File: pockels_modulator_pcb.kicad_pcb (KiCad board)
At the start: 2 copper layers, 39.4 x 23.8 mm, 11 parts, among them J1 Conn_Coaxial

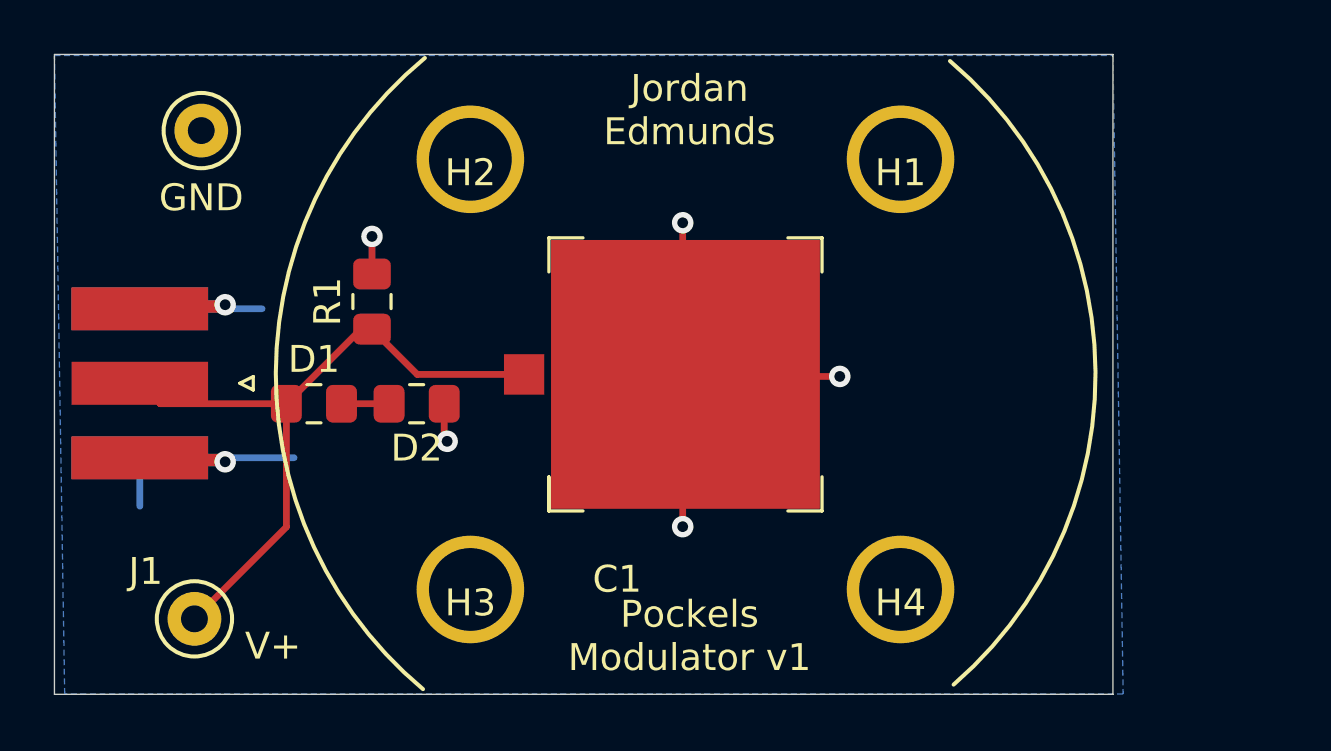
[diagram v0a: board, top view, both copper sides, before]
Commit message: revised pockels modulator PCB to include thermal vias, chip for thermal sensing, SMD connector
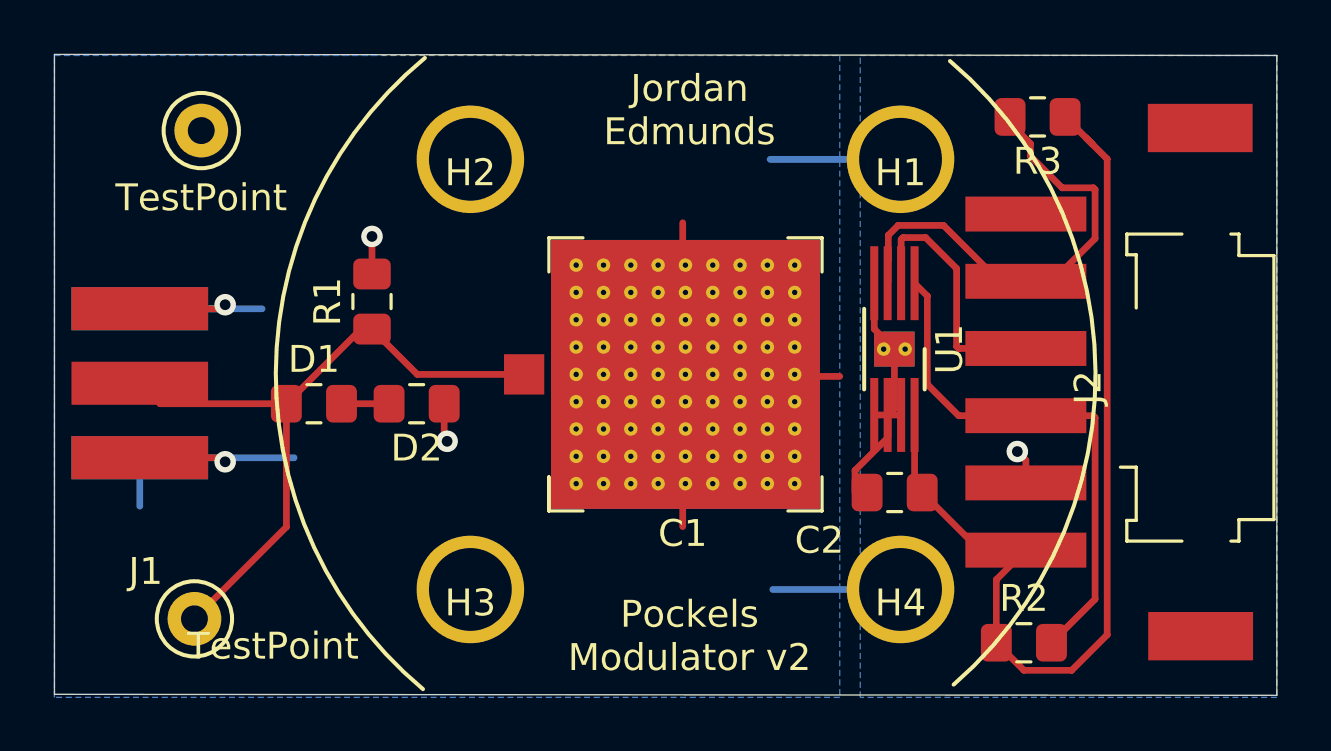
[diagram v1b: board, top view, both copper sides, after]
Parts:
- added C2: 100nF, Capacitor_SMD:C_0805_2012Metric_Pad1.15x1.40mm_HandSolder, F.Cu at (207.8, 104.4)
- added J2: Conn_01x06_Male, my_library_foot:S6B-XH-SM4-TB, F.Cu at (219.2, 109.7)
- added R2: 10k, Resistor_SMD:R_0805_2012Metric_Pad1.15x1.40mm_HandSolder, F.Cu at (212.6, 110.0)
- added R3: 10k, Resistor_SMD:R_0805_2012Metric_Pad1.15x1.40mm_HandSolder, F.Cu at (213.1, 90.4)
- added U1: MCP9804_DFN, Package_DFN_QFN:DFN-8-1EP_3x2mm_P0.5mm_EP1.3x1.5mm_HandSolder, F.Cu at (207.8, 99.1)
- C1: footprint my_library_foot:pockels_chip_10mm -> my_library_foot:pockels_chip_10mm_thermal
- TP1: value V+ -> TestPoint
- TP2: value GND -> TestPoint
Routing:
- net VDD: track 0.00 -> 37.5 mm
- net /SDA: track 0.00 -> 19.8 mm
- net /ALT: track 0.00 -> 17.7 mm
- net GNDD: track 0.00 -> 11.0 mm, vias 0 -> 1
- net /SCL: track 0.00 -> 9.70 mm
- net GND: track 41.4 -> 51.0 mm, vias 7 -> 4
- added copper zone on B.Cu, net GNDD
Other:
- board size 39.4 x 23.8 mm -> 45.5 x 23.8 mm
- board text added: "Pockels Modulator v2"
- board text removed: "Pockels Modulator v1"

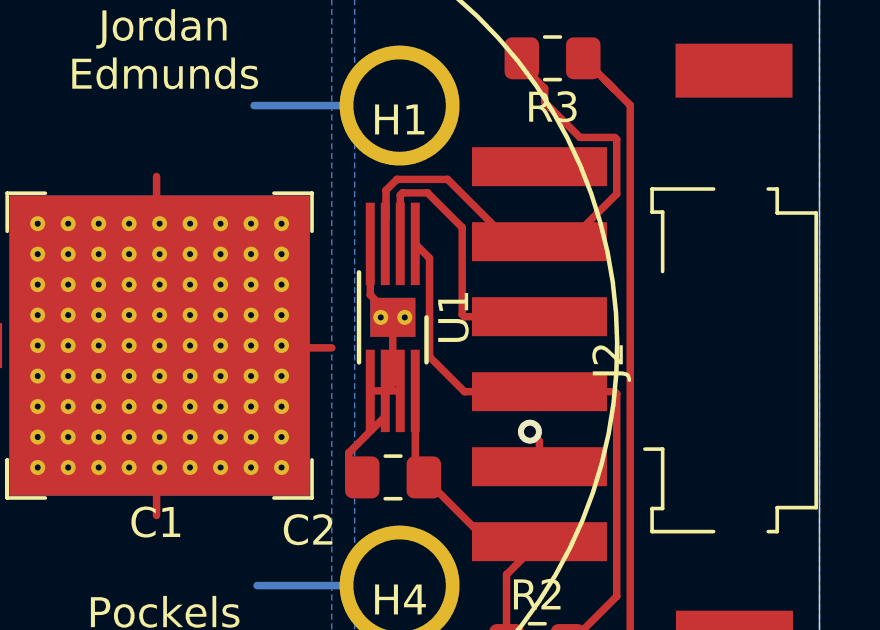
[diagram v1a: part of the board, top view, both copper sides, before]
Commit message: tweaked PCB in a manner I don't remember how. This is why you commit immediately after working.
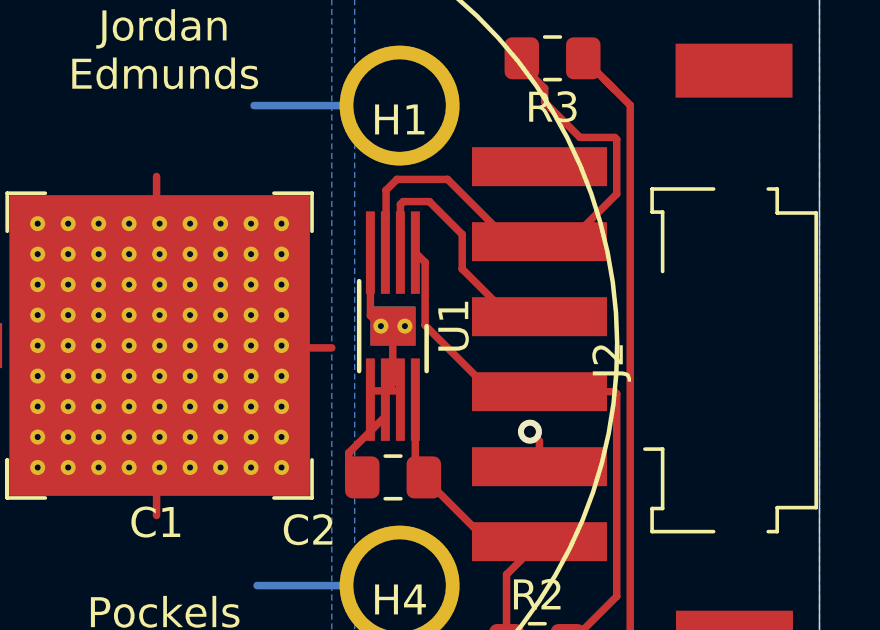
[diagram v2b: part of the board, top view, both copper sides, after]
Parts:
- moved U1 0.29 mm to (207.8, 99.4)
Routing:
- net /SCL: track 9.70 -> 8.55 mm
- net /SDA: track 19.8 -> 18.9 mm

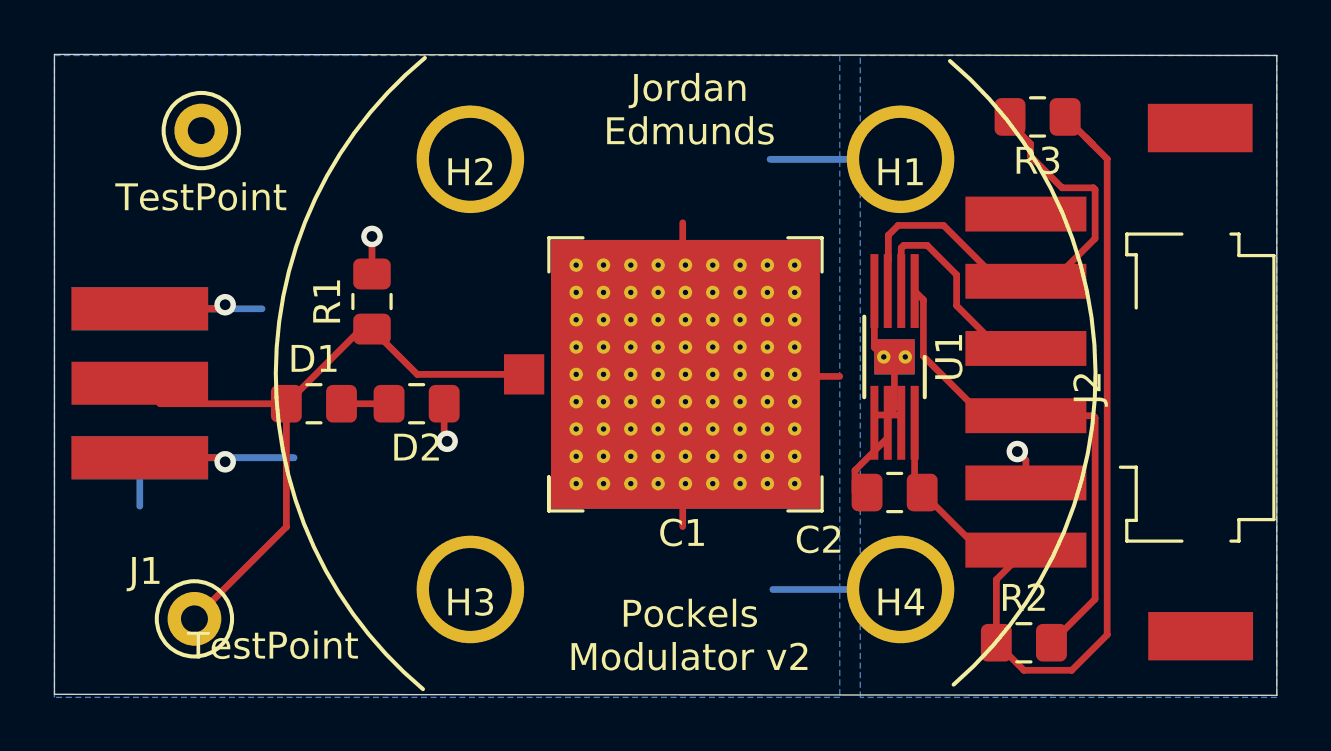
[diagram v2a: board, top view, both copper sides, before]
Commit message: updated for new 5mm chips to version 3
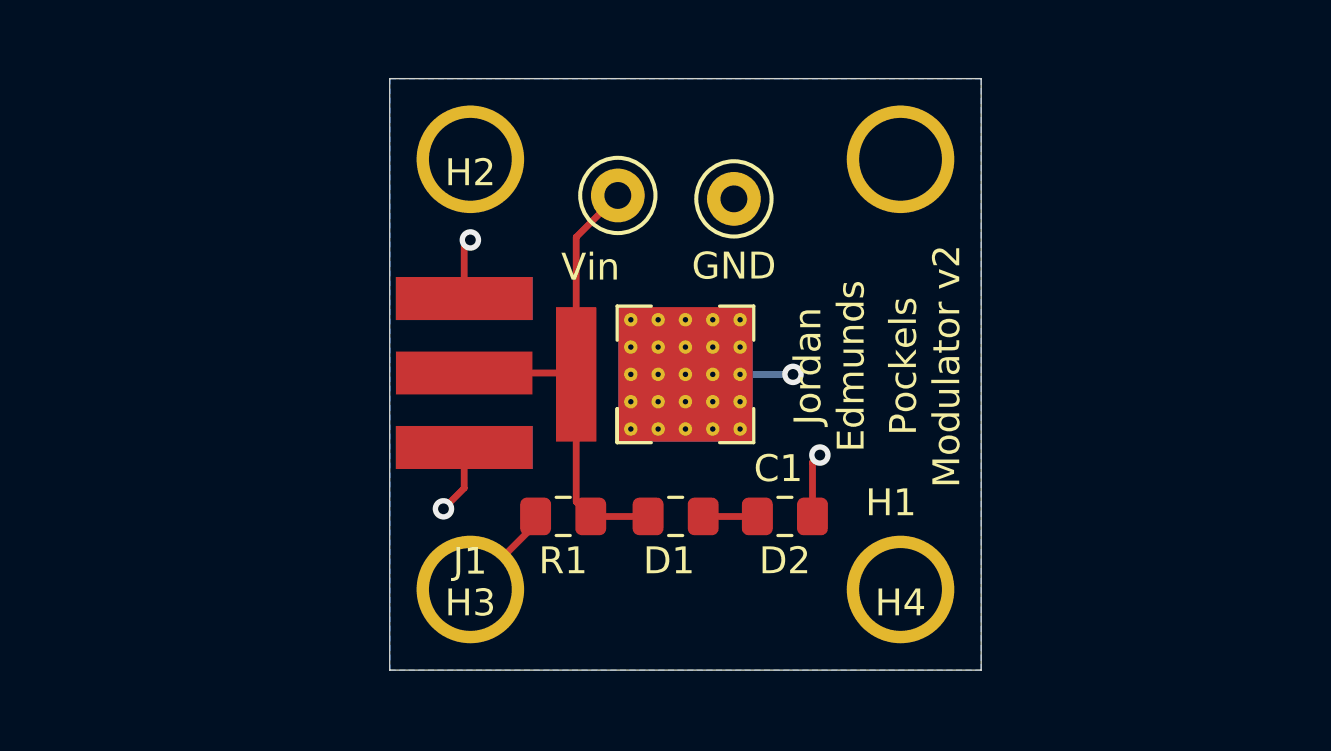
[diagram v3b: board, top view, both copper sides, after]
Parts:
- removed C2: 100nF, Capacitor_SMD:C_0805_2012Metric_Pad1.15x1.40mm_HandSolder
- removed J2: Conn_01x06_Male, my_library_foot:S6B-XH-SM4-TB
- removed R2, R3: 10k, Resistor_SMD:R_0805_2012Metric_Pad1.15x1.40mm_HandSolder
- removed U1: MCP9804_DFN, Package_DFN_QFN:DFN-8-1EP_3x2mm_P0.5mm_EP1.3x1.5mm_HandSolder
- C1: footprint my_library_foot:pockels_chip_10mm_thermal -> my_library_foot:pockels_chip_5mm_thermal
- TP1: value TestPoint -> Vin
- TP2: value TestPoint -> GND
- moved TP1 22.3 mm to (197.5, 93.3)
- moved TP2 20.0 mm to (201.8, 93.5)
- moved D2 14.3 mm to (203.7, 105.3)
- moved D1 14.1 mm to (199.6, 105.3)
- moved J1 12.1 mm to (193.5, 99.9)
- moved R1 10.7 mm to (195.5, 105.3), turned to 180 degrees
- moved H1 7.48 mm to (208.8, 99.4)
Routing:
- net VDD: track 37.5 -> 0.00 mm
- net GND: track 51.0 -> 15.4 mm
- net /SDA: track 18.9 -> 0.00 mm
- net /ALT: track 17.7 -> 0.00 mm
- net GNDD: track 10.8 -> 0.00 mm, vias 1 -> 0
- net /SCL: track 8.55 -> 0.00 mm
- net Net-(C1-Pad1): track 25.9 -> 19.1 mm
- removed copper zone on B.Cu, net GNDD
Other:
- board size 45.5 x 23.8 mm -> 22 x 22 mm
